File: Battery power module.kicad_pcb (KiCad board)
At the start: 2 copper layers, 20 x 20 mm, 14 parts, among them J1 USB_C_Receptacle_PowerOnly_6P, J2 Conn_01x02, U1 BQ24090DGQ

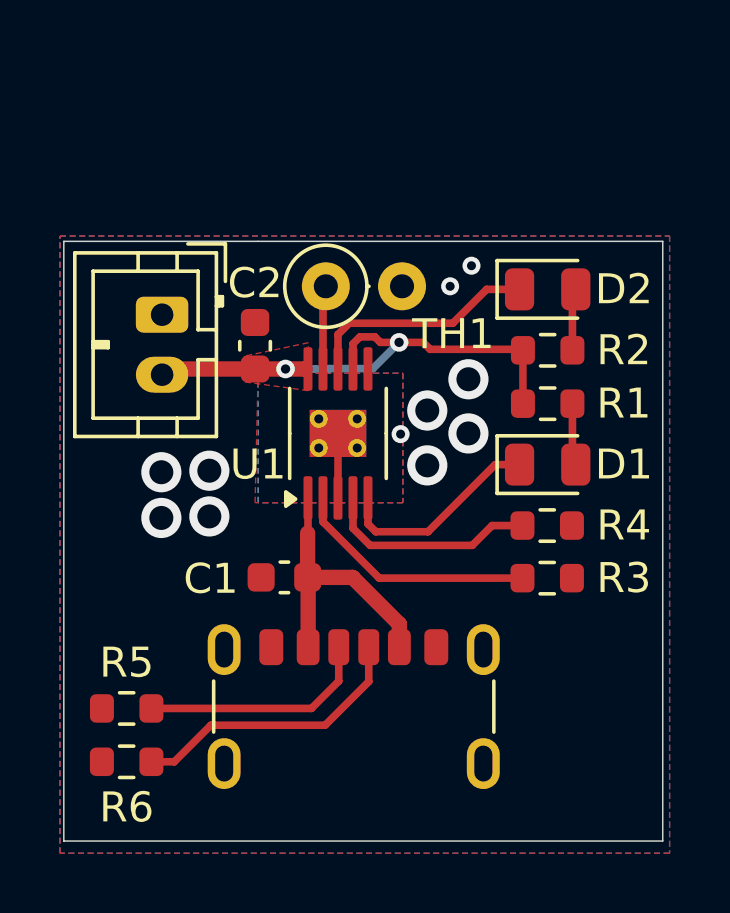
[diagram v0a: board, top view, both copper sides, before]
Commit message: Add TVS & finish ver. 1.0
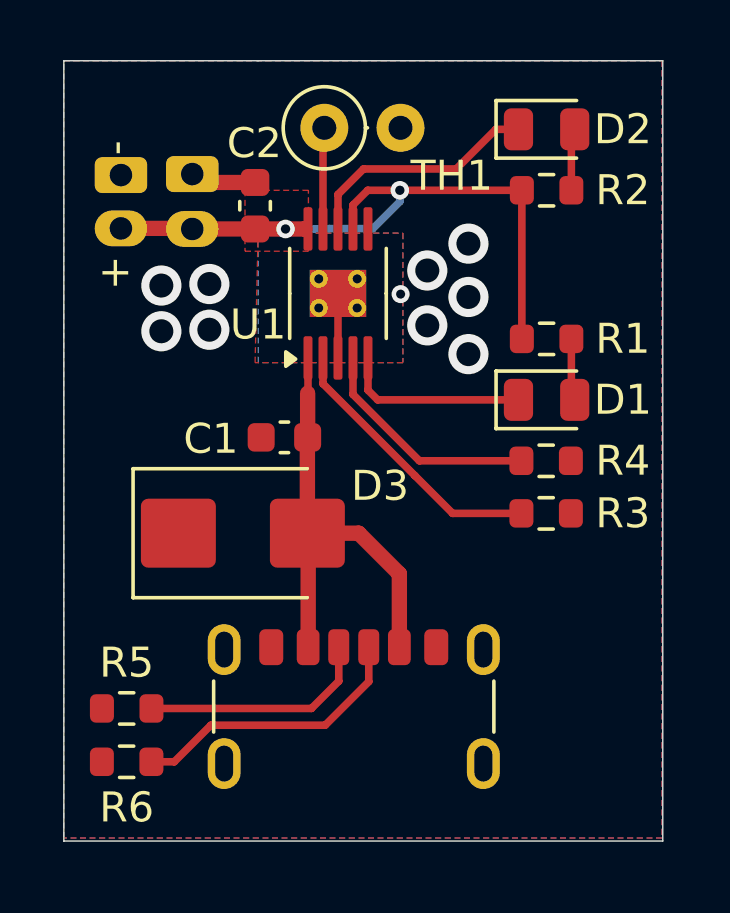
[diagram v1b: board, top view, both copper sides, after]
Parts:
- added ?: , , F.Cu at (121.9, 97.8)
- added ?: , , F.Cu at (121.9, 99.6)
- added D3: D_TVS, Diode_SMD:D_SMB, F.Cu at (126.0, 109.7)
- moved R2 5.33 mm to (136.1, 98.3)
- moved D2 5.33 mm to (136.1, 96.3)
- moved TH1 5.28 mm to (128.7, 96.2)
- moved J2 4.79 mm to (124.3, 97.8)
- moved C1 4.67 mm to (127.4, 106.5)
- moved C2 4.67 mm to (126.4, 98.8)
- moved U1 4.67 mm to (129.2, 101.7)
- moved R3 2.16 mm to (136.1, 109.1)
- moved R4 2.16 mm to (136.1, 107.3)
- moved D1 2.16 mm to (136.1, 105.3)
- moved R1 2.16 mm to (136.1, 103.3)
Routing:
- net /VBUS: track 9.46 -> 15.8 mm
- net VCC: track 17.5 -> 22.4 mm
- net GND: track 2.15 -> 4.36 mm, vias 11 -> 10
- net /ISET: track 8.22 -> 9.26 mm
- net /PG: track 6.95 -> 6.22 mm
- net /PRETERM: track 7.17 -> 7.75 mm
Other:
- board size 20 x 20 mm -> 20 x 26 mm
- board text added: "+"
- board text added: "-"
- board text added: "Battery power module by hugo2080 2025"
- board text removed: "Battery power module by Hubert Gnyp 2025"
